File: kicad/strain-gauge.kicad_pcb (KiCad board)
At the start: 2 copper layers, 16 parts, among them J1 Left, J2 Right, U1 ADS8691IPWR, U2 TMUX131RMG, U3 SN74HCS72QDRQ1, U4 74AHC1G00, U5 AD8421

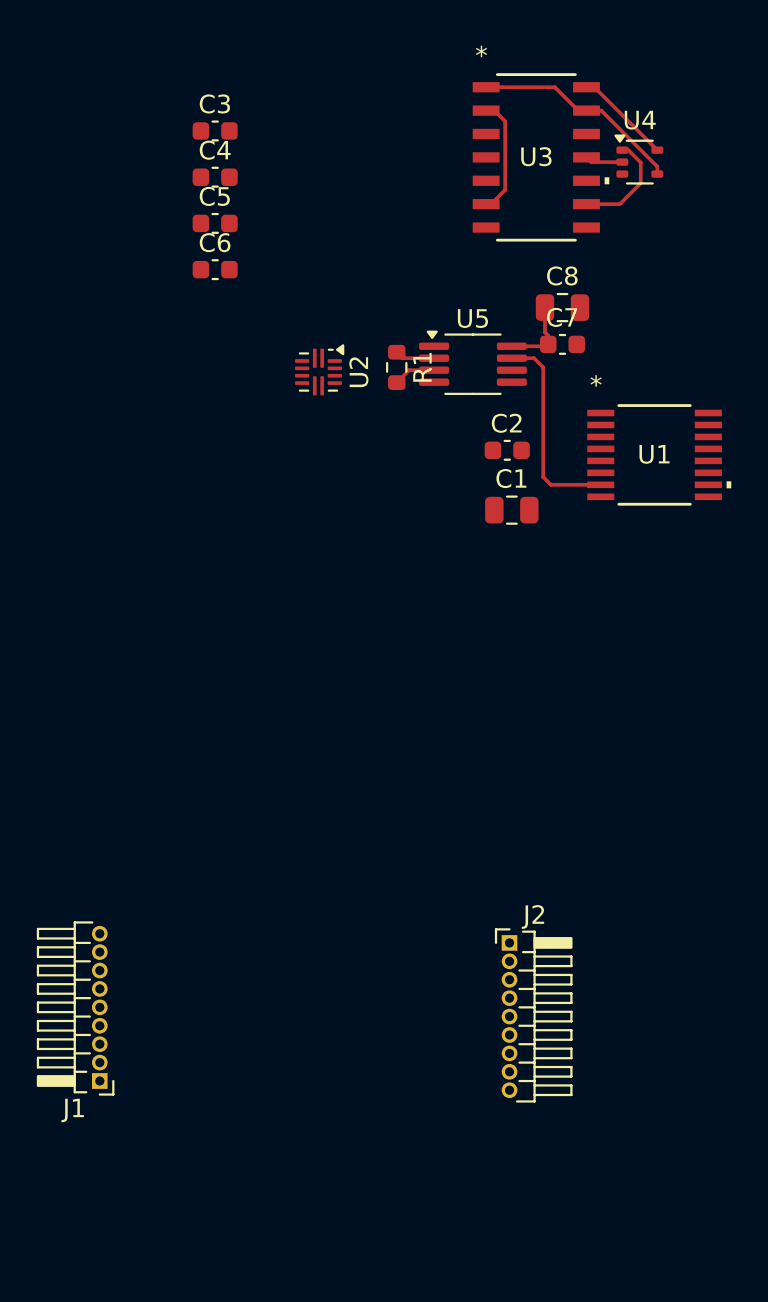
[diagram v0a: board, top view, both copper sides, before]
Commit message: started routing pcb
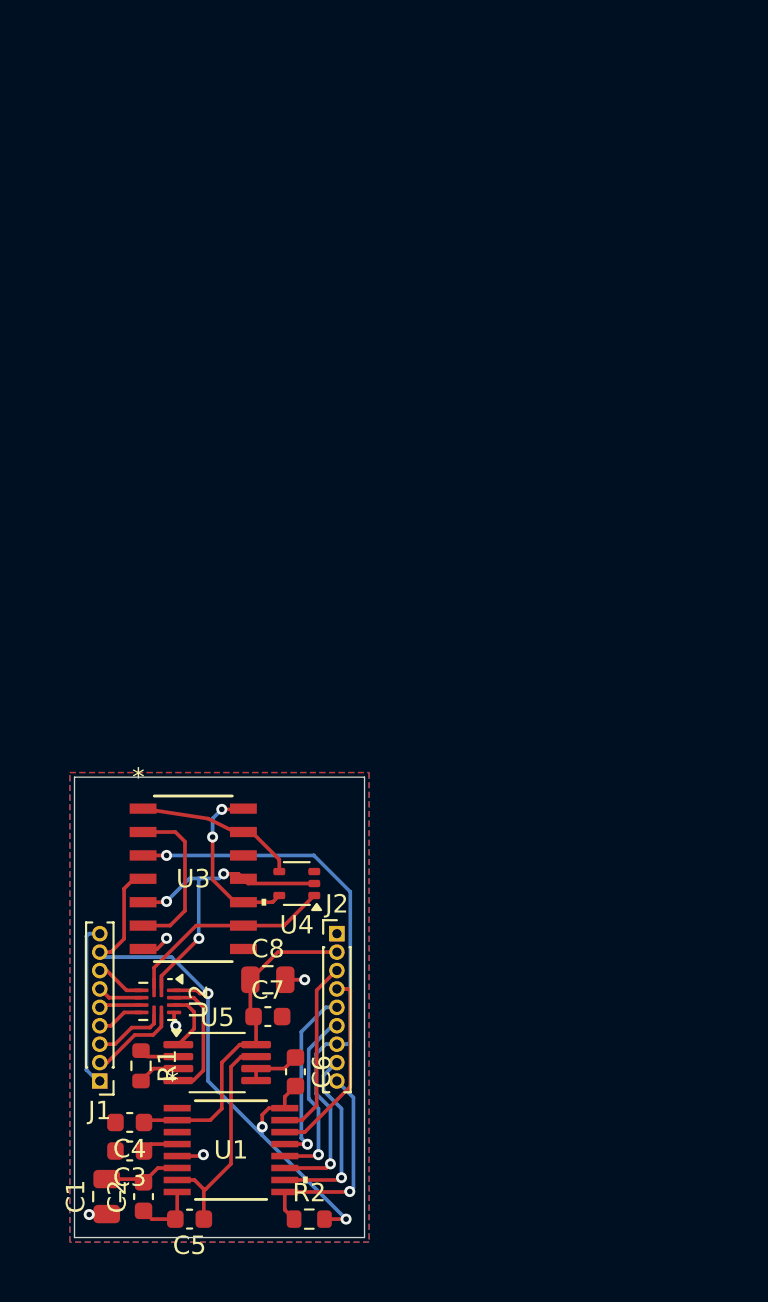
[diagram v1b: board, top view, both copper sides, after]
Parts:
- added R2: 100k, Resistor_SMD:R_0603_1608Metric, F.Cu at (97.0, 139.2)
- J1, J2: footprint Connector_PinHeader_1.00mm:PinHeader_1x09_P1.00mm_Horizontal -> Connector_PinHeader_1.00mm:PinHeader_1x09_P1.00mm_Vertical
- moved C3 55.6 mm to (87.2, 135.6), turned to 180 degrees
- moved C5 54.1 mm to (90.5, 139.2), turned to 180 degrees
- moved C4 51.5 mm to (87.2, 134.0), turned to 180 degrees
- moved C2 45.1 mm to (88.0, 138.0), turned to 90 degrees
- moved U1 44.2 mm to (92.8, 135.5)
- moved C6 43.8 mm to (96.2, 131.2), turned to -90 degrees
- moved U3 43.4 mm to (90.7, 120.8)
- moved U4 43.4 mm to (96.3, 121.0), turned to 180 degrees
- moved C1 43.3 mm to (86.0, 138.0), turned to 90 degrees
- moved R1 40.4 mm to (87.9, 130.9)
- moved U5 40.4 mm to (92.0, 130.8)
- moved C7 39.9 mm to (94.8, 128.2)
- moved C8 39.9 mm to (94.8, 126.2)
- moved U2 35.3 mm to (88.8, 127.4)
- moved J2 9.39 mm to (98.5, 123.8)
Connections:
- J1 pad 1: unconnected-(J1-Pin_1-Pad1) -> GND
- J1 pad 2: unconnected-(J1-Pin_2-Pad2) -> /Multiplexer/A_IN_N1
- J1 pad 3: unconnected-(J1-Pin_3-Pad3) -> /Multiplexer/A_IN_P1
- J1 pad 4: unconnected-(J1-Pin_4-Pad4) -> /Multiplexer/A_IN_N3
- J1 pad 5: unconnected-(J1-Pin_5-Pad5) -> /Multiplexer/A_IN_P3
- J1 pad 6: unconnected-(J1-Pin_6-Pad6) -> /Multiplexer/A_IN_N2
- J1 pad 7: unconnected-(J1-Pin_7-Pad7) -> /Multiplexer/A_IN_P2
- J1 pad 8: unconnected-(J1-Pin_8-Pad8) -> +3.3V
- J1 pad 9: unconnected-(J1-Pin_9-Pad9) -> GND
- J2 pad 1: unconnected-(J2-Pin_1-Pad1) -> GND
- J2 pad 2: unconnected-(J2-Pin_2-Pad2) -> +5V
- J2 pad 3: unconnected-(J2-Pin_3-Pad3) -> /ADC/RVS
- J2 pad 4: unconnected-(J2-Pin_4-Pad4) -> /ADC/SDO-1
- J2 pad 5: unconnected-(J2-Pin_5-Pad5) -> /ADC/SDO-0
- J2 pad 6: unconnected-(J2-Pin_6-Pad6) -> /ADC/SCLK
- J2 pad 7: unconnected-(J2-Pin_7-Pad7) -> /ADC/~{CS}
- J2 pad 8: unconnected-(J2-Pin_8-Pad8) -> /ADC/SDI
- J2 pad 9: unconnected-(J2-Pin_9-Pad9) -> /ADC/~{RST}
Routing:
- net +3.3V: track 5.71 -> 44.7 mm, vias 0 -> 5
- net /ADC/~{CS}: track 0.00 -> 31.2 mm, vias 0 -> 2
- net GND: track 0.00 -> 21.1 mm, vias 0 -> 5
- net /Counter/SEL0: track 2.05 -> 16.9 mm, vias 0 -> 3
- net +5V: track 4.09 -> 18.3 mm
- net /ADC/~{RST}: track 0.00 -> 11.7 mm, vias 0 -> 1
- net /ADC/SDO-1: track 0.00 -> 10.5 mm
- net /ADC/SDI: track 0.00 -> 10.1 mm, vias 0 -> 1
- net /ADC/SDO-0: track 0.00 -> 9.95 mm, vias 0 -> 1
- net /ADC/RVS: track 0.00 -> 9.86 mm
- net /ADC/SCLK: track 0.00 -> 9.86 mm, vias 0 -> 1
- net /Amplifier/A_IN_P: track 0.00 -> 6.82 mm
- net /Counter/SEL1: track 5.82 -> 11.4 mm
- net /Multiplexer/A_IN_N1: track 0.00 -> 4.78 mm
- net Net-(U1-REFCAP): track 0.00 -> 4.22 mm
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- added copper zone on B.Cu, net GND
- added copper zone on F.Cu, net GND
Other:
- board outline added: 15.8 x 25 mm

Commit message: the routing is awful but also done
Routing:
- net +3.3V: track 44.7 -> 58.3 mm
- net Net-(U3-2D): track 0.00 -> 12.0 mm
- net GND: track 21.1 -> 24.4 mm, vias 5 -> 7
- net Net-(U3-~{1CLR}): track 8.88 -> 11.9 mm
- net /Counter/SEL0: track 16.9 -> 17.7 mm
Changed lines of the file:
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@@
 		(tags "capacitor")
 		(property "Reference" "C5"
-			(at 0 -1.43 0)
+			(at -2.5 0 0)
 			(layer "F.SilkS")
 			(effects
@@
 		)
 		(fp_text user "*"
-			(at -2.97815 -5.5118 0)
+			(at -4.450035 -4.269565 0)
 			(layer "F.SilkS")
 			(effects
@@
 		)
 		(fp_text user "*"
-			(at -2.97815 -5.5118 0)
+			(at -4.450035 -4.269565 0)
 			(unlocked yes)
 			(layer "F.SilkS")
@@
 	)
 	(segment
+		(start 96.6 120.375565)
+		(end 96.5 120.475565)
+		(width 0.2)
+		(layer "F.Cu")
+		(net 1)
+	)
+	(segment
 		(start 85.075 138.975)
 		(end 85.05 139)
@@
 	)
 	(segment
+		(start 85.625 123.75)
+		(end 85.625 123.625)
+		(width 0.2)
+		(layer "F.Cu")
+		(net 1)
+	)
+	(segment
 		(start 94.1125 131.075)
 		(end 94.1125 131.725)
@@
 	)
 	(segment
+		(start 97.270435 120.375565)
+		(end 96.6 120.375565)
+		(width 0.2)
+		(layer "F.Cu")
+		(net 1)
+	)
+	(segment
 		(start 89.829 137.774999)
 		(end 89.829 139.146)
@@
 	)
 	(segment
+		(start 89.829 134.525001)
+		(end 91.025001 134.525001)
+		(width 0.2)
+		(layer "F.Cu")
+		(net 1)
+	)
+	(segment
+		(start 91.025001 134.525001)
+		(end 91.25 134.75)
+		(width 0.2)
+		(layer "F.Cu")
+		(net 1)
+	)
+	(segment
 		(start 88.45 139.25)
 		(end 88 138.8)
@@
 	)
 	(segment
+		(start 85.625 123.625)
+		(end 86.25 123)
+		(width 0.2)
+		(layer "F.Cu")
+		(net 1)
+	)
+	(segment
 		(start 88.739005 124.579565)
 		(end 87.975885 124.579565)
@@
 	)
 	(via
+		(at 86.25 123)
+		(size 0.6)
+		(drill 0.3)
+		(layers "F.Cu" "B.Cu")
+		(net 1)
+	)
+	(via
+		(at 96.5 120.475565)
+		(size 0.6)
+		(drill 0.3)
+		(layers "F.Cu" "B.Cu")
+		(net 1)
+	)
+	(via
 		(at 89.75 128.75)
 		(size 0.6)
@@
 	)
 	(segment
-		(start 93.424185 122.039565)
-		(end 92.973335 122.039565)
+		(start 90.601 118.899)
+		(end 91.25 118.25)
 		(width 0.2)
 		(layer "F.Cu")
@@
 	)
 	(segment
+		(start 91.539565 122.039565)
+		(end 90.601 121.101)
+		(width 0.2)
+		(layer "F.Cu")
+		(net 6)
+	)
+	(segment
 		(start 95.671 133.225001)
 		(end 95.671 132.604)
@@
 	)
 	(segment
+		(start 92.893785 116.429165)
+		(end 86.994635 116.429165)
+		(width 0.2)
+		(layer "F.Cu")
+		(net 6)
+	)
+	(segment
+		(start 86.944635 116.479165)
+		(end 86.944635 121.305365)
+		(width 0.2)
+		(layer "F.Cu")
+		(net 6)
+	)
+	(segment
 		(start 94.446464 134.238021)
 		(end 94.446464 133.583138)
@@
 	)
 	(segment
-		(start 93.38375 117)
-		(end 93.424185 116.959565)
+		(start 86.994635 116.429165)
+		(end 86.944635 116.479165)
 		(width 0.2)
 		(layer "F.Cu")
@@
 	)
 	(segment
+		(start 93.424185 116.959565)
+		(end 92.893785 116.429165)
+		(width 0.2)
+		(layer "F.Cu")
+		(net 6)
+	)
+	(segment
+		(start 90.601 121.101)
+		(end 90.601 118.899)
+		(width 0.2)
+		(layer "F.Cu")
+		(net 6)
+	)
+	(segment
+		(start 91.75 117)
+		(end 93.38375 117)
+		(width 0.2)
+		(layer "F.Cu")
+		(net 6)
+	)
+	(segment
 		(start 95.006435 122.039565)
 		(end 95.370435 121.675565)
@@
 	)
 	(segment
-		(start 91.75 120.81623)
-		(end 91.75 118.5)
+		(start 93.424185 122.039565)
+		(end 91.539565 122.039565)
 		(width 0.2)
 		(layer "F.Cu")
@@
 	)
 	(segment
-		(start 86.944635 121.305365)
-		(end 87.480435 120.769565)
+		(start 93.38375 117)
+		(end 93.424185 116.959565)
 		(width 0.2)
 		(layer "F.Cu")
@@
 	)
 	(segment
-		(start 92.973335 122.039565)
-		(end 91.75 120.81623)
+		(start 86.944635 121.305365)
+		(end 87.480435 120.769565)
 		(width 0.2)
 		(layer "F.Cu")
@@
 		(net 6)
 	)
-	(segment
-		(start 92.25 117)
-		(end 93.38375 117)
-		(width 0.2)
-		(layer "F.Cu")
-		(net 6)
-	)
 	(via
-		(at 91.75 118.5)
+		(at 91.25 118.25)
 		(size 0.6)
 		(drill 0.3)
@@
 	)
 	(via
-		(at 92.25 117)
+		(at 91.75 117)
 		(size 0.6)
 		(drill 0.3)
@@
 	)
 	(segment
-		(start 91.75 117.5)
-		(end 92.25 117)
+		(start 91.5 127)
+		(end 89.524 125.024)
 		(width 0.2)
 		(layer "B.Cu")
@@
 	)
 	(segment
-		(start 91.5 127)
-		(end 89.524 125.024)
+		(start 94.446464 134.696464)
+		(end 94.446464 134.238021)
 		(width 0.2)
 		(layer "B.Cu")
@@
 	)
 	(segment
-		(start 94.446464 134.696464)
-		(end 94.446464 134.238021)
+		(start 91.25 117.5)
+		(end 91.75 117)
 		(width 0.2)
 		(layer "B.Cu")
@@
 	)
 	(segment
+		(start 91.25 118.25)
+		(end 91.25 117.5)
+		(width 0.2)
+		(layer "B.Cu")
+		(net 6)
+	)
+	(segment
 		(start 89.524 125.024)
 		(end 85.899 125.024)
@@
 	)
 	(segment
-		(start 91.75 118.5)
-		(end 91.75 117.5)
-		(width 0.2)
-		(layer "B.Cu")
-		(net 6)
-	)
-	(segment
 		(start 89.8875 130.425)
 		(end 88.1875 130.425)
@@
 	)
 	(segment
-		(start 92.35 120.5)
-		(end 93.15462 120.5)
+		(start 91.019565 120.769565)
+		(end 93.424185 120.769565)
 		(width 0.2)
 		(layer "F.Cu")
@@
 	)
 	(segment
-		(start 93.15462 120.5)
-		(end 93.424185 120.769565)
-		(width 0.2)
-		(layer "F.Cu")
-		(net 25)
-	)
-	(segment
 		(start 93.680185 121.025565)
 		(end 97.270435 121.025565)
@@
 	)
 	(segment
+		(start 91.5 120.769565)
+		(end 91.019565 120.769565)
+		(width 0.2)
+		(layer "F.Cu")
+		(net 25)
+	)
+	(segment
 		(start 93.424185 120.769565)
 		(end 93.680185 121.025565)
@@
 	)
 	(via
-		(at 92.35 120.5)
+		(at 91.5 120.769565)
 		(size 0.6)
 		(drill 0.3)
@@
 	(segment
 		(start 91 124)
-		(end 91 120.75)
-		(width 0.2)
-		(layer "B.Cu")
-		(net 25)
-	)
-	(segment
-		(start 89.25 122)
-		(end 90.5 120.75)
+		(end 91.007815 124.007815)
 		(width 0.2)
 		(layer "B.Cu")
@@
 	(segment
 		(start 90.5 120.75)
-		(end 91 120.75)
-		(width 0.2)
-		(layer "B.Cu")
-		(net 25)
-	)
-	(segment
-		(start 92.1 120.75)
-		(end 92.35 120.5)
+		(end 89.25 122)
 		(width 0.2)
 		(layer "B.Cu")
@@
 	)
 	(segment
-		(start 91 120.75)
-		(end 92.1 120.75)
+		(start 91.5 120.769565)
+		(end 91 124)
 		(width 0.2)
 		(layer "B.Cu")
@@
 	)
 	(segment
-		(start 91.007815 124.007815)
-		(end 91 124)
+		(start 91.5 120.769565)
+		(end 90.5 120.75)
 		(width 0.2)
 		(layer "B.Cu")
@@
 	)
 	(segment
+		(start 93.424185 124.579565)
+		(end 93.60475 124.399)
+		(width 0.2)
+		(layer "F.Cu")
+		(net 27)
+	)
+	(segment
+		(start 95.37116 124.399)
+		(end 97.846435 121.923725)
+		(width 0.2)
+		(layer "F.Cu")
+		(net 27)
+	)
+	(segment
+		(start 97.846435 120.127405)
+		(end 97.218595 119.499565)
+		(width 0.2)
+		(layer "F.Cu")
+		(net 27)
+	)
+	(segment
+		(start 97.846435 121.923725)
+		(end 97.846435 120.127405)
+		(width 0.2)
+		(layer "F.Cu")
+		(net 27)
+	)
+	(segment
+		(start 93.60475 124.399)
+		(end 95.37116 124.399)
+		(width 0.2)
+		(layer "F.Cu")
+		(net 27)
+	)
+	(segment
+		(start 97.218595 119.499565)
+		(end 93.424185 119.499565)
+		(width 0.2)
+		(layer "F.Cu")
+		(net 27)
+	)
+	(segment
 		(start 92.973335 118.229565)
 		(end 91.5 117.5)
@@
 	)
 	(segment
-		(start 95.370435 119.724965)
-		(end 93.875035 118.229565)
+		(start 92.260835 120.239165)
+		(end 92.25 120.25)
+		(width 0.2)
+		(layer "F.Cu")
+		(net 28)
+	)
+	(segment
+		(start 92.25 120.25)
+		(end 92.25 119.25)
+		(width 0.2)
+		(layer "F.Cu")
+		(net 28)
+	)
+	(segment
+		(start 95.234035 120.239165)
+		(end 92.260835 120.239165)
+		(width 0.2)
+		(layer "F.Cu")
+		(net 28)
+	)
+	(segment
+		(start 95.370435 120.375565)
+		(end 95.234035 120.239165)
 		(width 0.2)
 		(layer "F.Cu")
@@
 	)
 	(segment
-		(start 95.370435 120.375565)
-		(end 95.370435 119.724965)
+		(start 92.25 119.25)
+		(end 93.270435 118.229565)
 		(width 0.2)
 		(layer "F.Cu")
@@
 		(net 28)
 	)
+	(segment
+		(start 93.270435 118.229565)
+		(end 93.424185 118.229565)
+		(width 0.2)
+		(layer "F.Cu")
+		(net 28)
+	)
 	(zone
 		(net 1)
@@
 		(layers "F.Cu" "B.Cu")
 		(hatch edge 0.5)
-		(connect_pads
+		(connect_pads thru_hole_only
 			(clearance 0.5)
 		)

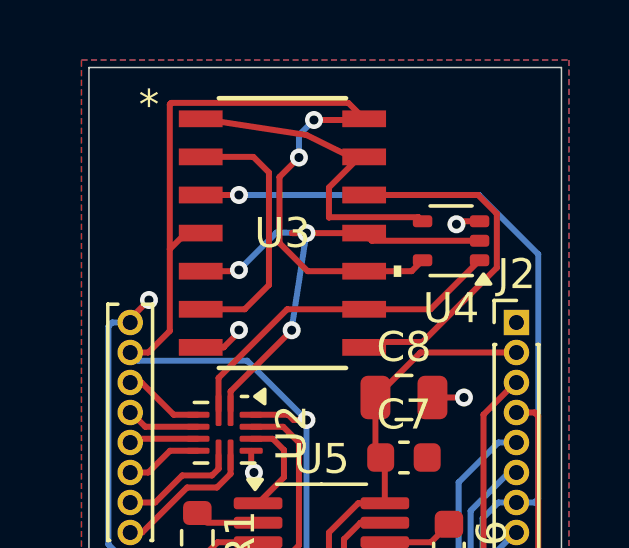
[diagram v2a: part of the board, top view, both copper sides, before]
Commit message: make the component values more visible on pcb
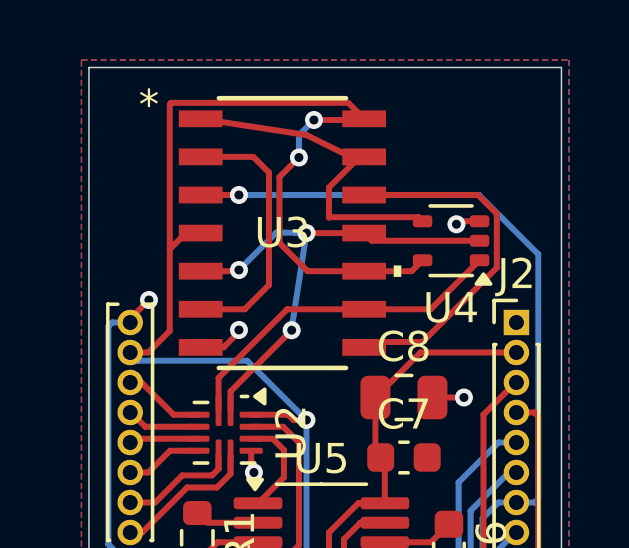
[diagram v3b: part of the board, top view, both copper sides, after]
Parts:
- R1: value 100 -> 100R
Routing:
- net /Counter/SEL0: track 17.7 -> 16.7 mm
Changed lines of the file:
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@@
 		)
 		(property "Value" "AD8421"
-			(at 0 2.45 0)
+			(at 11.25 -0.5 0)
 			(layer "F.Fab")
 			(effects
@@
 		)
 		(property "Value" "0.1 uF"
-			(at 0 1.43 0)
+			(at 8 0 0)
 			(layer "F.Fab")
 			(effects
@@
 		)
 		(property "Value" "1 uF"
-			(at 0 1.43 90)
+			(at -3.975 -0.25 90)
 			(layer "F.Fab")
 			(effects
@@
 		)
 		(property "Value" "1 uF"
-			(at 0 1.43 0)
+			(at 4.75 0 0)
 			(layer "F.Fab")
 			(effects
@@
 		)
 		(property "Value" "1 uF"
-			(at 0 1.43 90)
+			(at 0.75 -5.75 0)
 			(layer "F.Fab")
 			(effects
@@
 		)
 		(property "Value" "Right"
-			(at 0 9.61 0)
+			(at 3.75 -0.5 0)
 			(layer "F.Fab")
 			(effects
@@
 		)
 		(property "Value" "TMUX131RMG"
-			(at 0 2.23 90)
+			(at -1.175565 9.770435 180)
 			(layer "F.Fab")
 			(effects
@@
 		)
 		(property "Value" "74AHC1G00"
-			(at 0 2 0)
+			(at -8.429565 0.275565 0)
 			(layer "F.Fab")
 			(effects
@@
 		)
 		(property "Value" "4.7 uF"
-			(at 0 1.43 0)
+			(at 5.5 0.05 0)
 			(layer "F.Fab")
 			(effects
@@
 		)
 		(property "Value" "1 uF"
-			(at 0 1.43 0)
+			(at 0 -1.75 0)
 			(layer "F.Fab")
 			(effects
@@
 		)
 		(property "Value" "SN74HCS72QDRQ1"
-			(at 0 0 0)
+			(at 0 -6.519565 0)
 			(unlocked yes)
 			(layer "F.Fab")
@@
 			)
 		)
-		(property "Value" "100"
-			(at 0 1.43 90)
+		(property "Value" "100R"
+			(at 0.075 5.6125 180)
 			(layer "F.Fab")
 			(effects
@@
 		)
 		(property "Value" "Left"
-			(at 0 9.61 180)
+			(at 2.875 8.5 180)
 			(layer "F.Fab")
 			(effects
@@
 		)
 		(property "Value" "10 uF"
-			(at 0 1.68 0)
+			(at 7.75 0.25 0)
 			(layer "F.Fab")
 			(effects
@@
 		)
 		(property "Value" "10 uF"
-			(at 0 1.68 90)
+			(at -4.475 0 90)
 			(layer "F.Fab")
 			(effects
@@
 	)
 	(segment
-		(start 91.019565 120.769565)
+		(start 91.5 120.769565)
 		(end 93.424185 120.769565)
 		(width 0.2)
@@
 		(width 0.2)
 		(layer "F.Cu")
-		(net 25)
-	)
-	(segment
-		(start 91.5 120.769565)
-		(end 91.019565 120.769565)
-		(width 0.2)
-		(layer "F.Cu")

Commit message: slightly better routing
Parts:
- R1: value 100R -> 100
- moved U4 1.48 mm to (97.7, 120.5)
- moved U3 0.76 mm to (91.2, 120.2), turned to 90 degrees
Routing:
- net /Counter/SEL1: track 11.4 -> 21.0 mm, vias 0 -> 3
- net Net-(U3-~{1CLR}): track 11.9 -> 17.8 mm
- net Net-(U3-2D): track 12.0 -> 6.31 mm
- net GND: track 24.4 -> 28.0 mm, vias 7 -> 12
- net /ADC/~{CS}: track 31.2 -> 28.1 mm
- net +3.3V: track 58.3 -> 60.5 mm
- net /Counter/SEL0: track 16.7 -> 18.1 mm, vias 3 -> 0
- net Net-(U3-1D): track 8.85 -> 8.74 mm, vias 0 -> 2

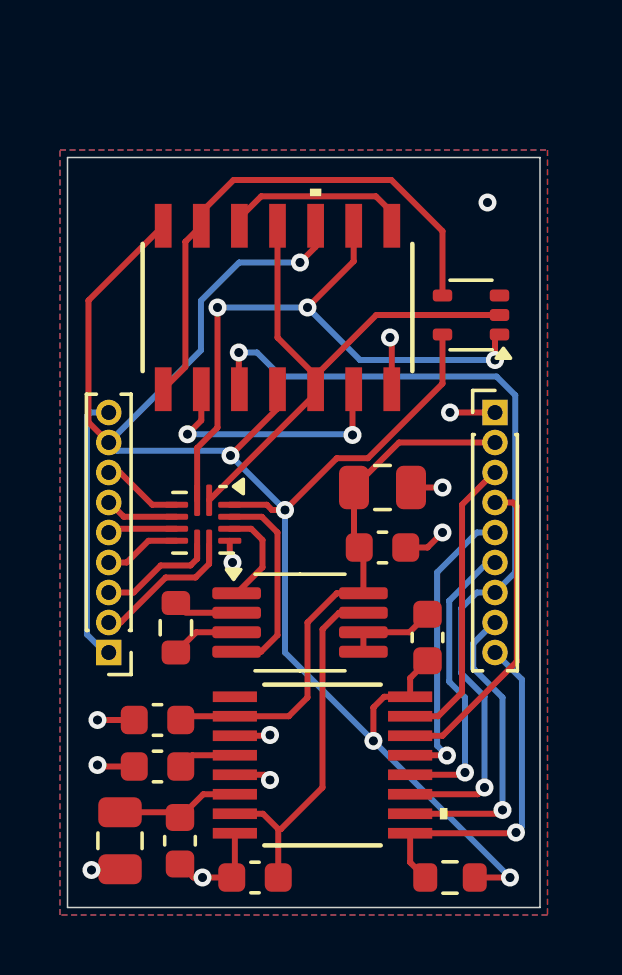
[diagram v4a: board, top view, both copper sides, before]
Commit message: moved traces
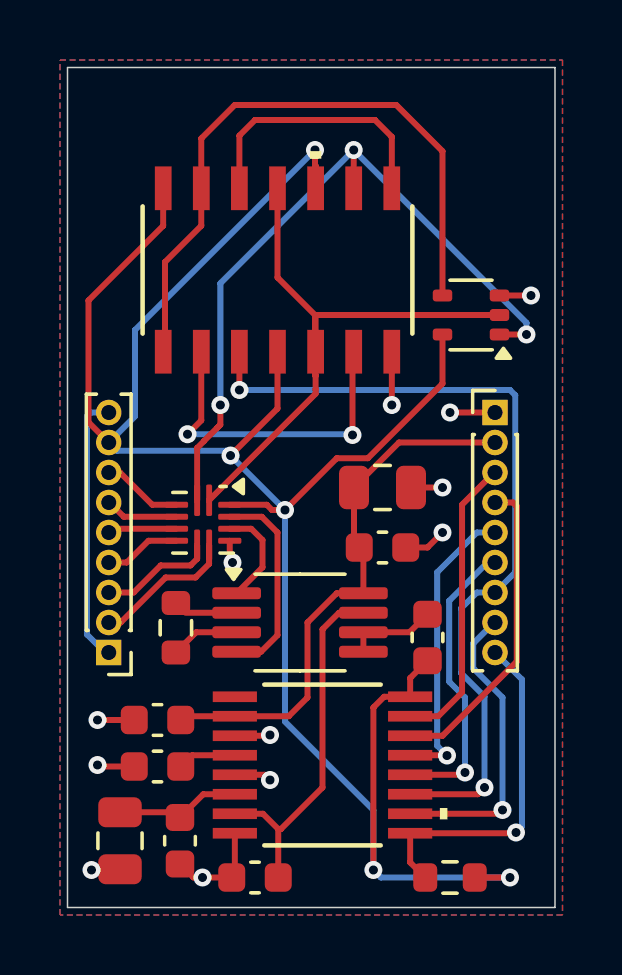
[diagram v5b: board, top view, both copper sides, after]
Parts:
- moved U3 1.25 mm to (91.2, 119.0)
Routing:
- net +3.3V: track 60.5 -> 73.2 mm
- net Net-(U3-~{1CLR}): track 17.8 -> 21.6 mm
- net /Counter/SEL1: track 21.0 -> 24.6 mm
- net Net-(U3-2D): track 6.31 -> 9.00 mm
- net Net-(U3-1D): track 8.74 -> 11.2 mm
- net /Counter/SEL0: track 18.1 -> 20.5 mm
- net GND: track 28.0 -> 28.8 mm
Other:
- board size 15.8 x 25 mm -> 16.2 x 28 mm
